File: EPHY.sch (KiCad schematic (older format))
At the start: 10 parts

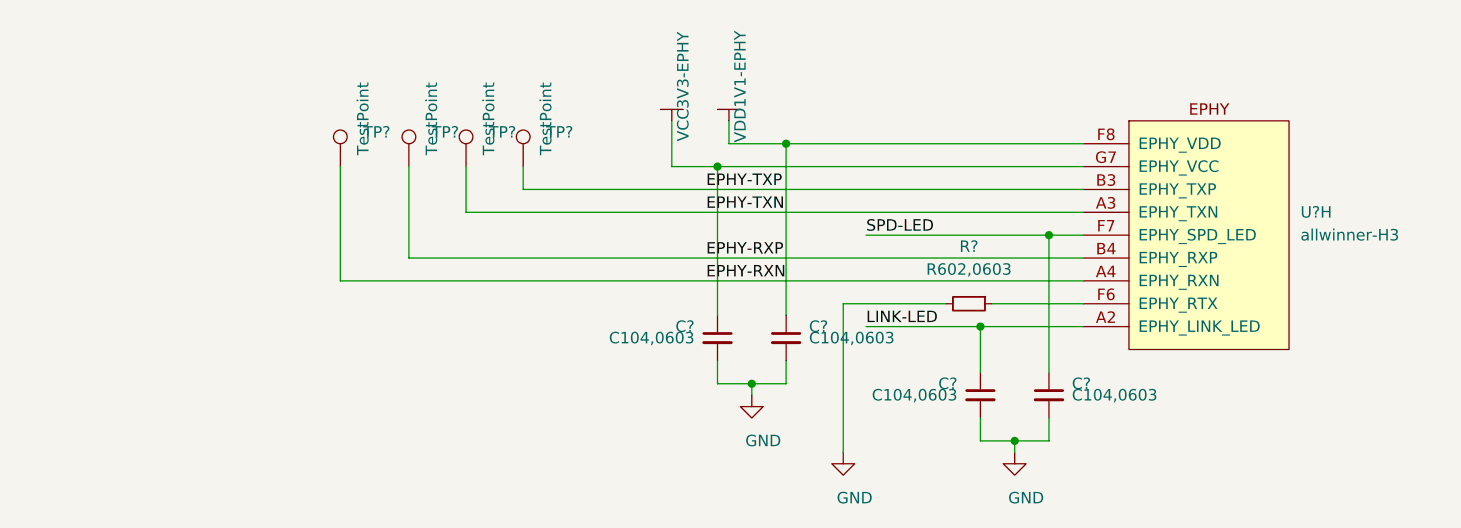
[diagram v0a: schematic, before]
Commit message: update test point,
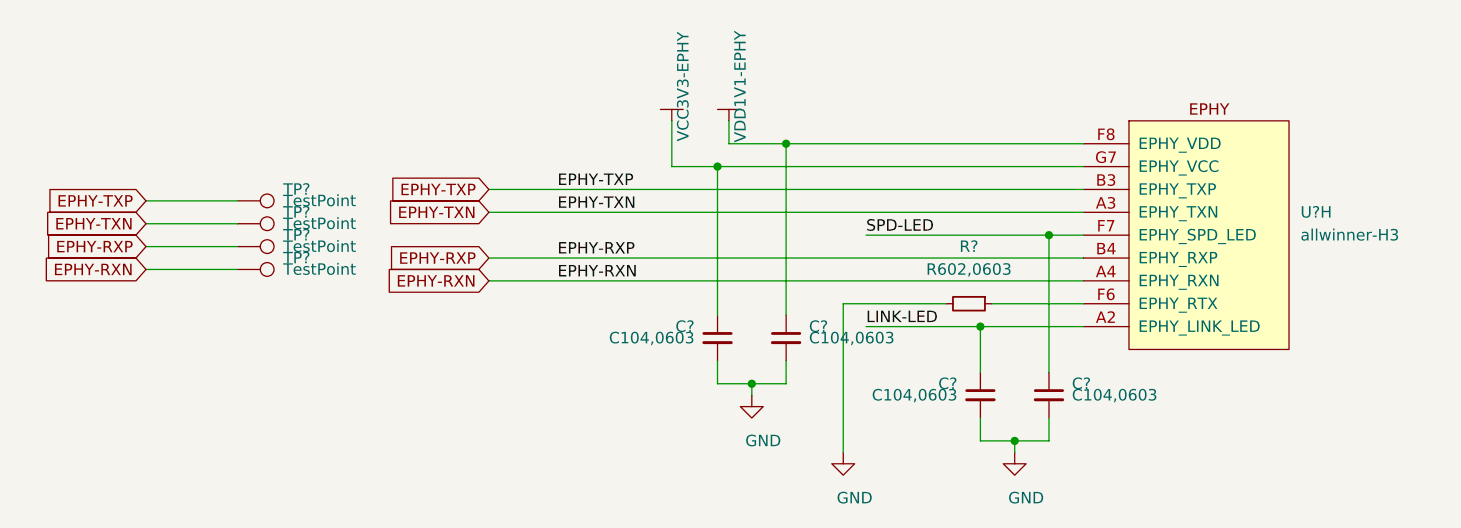
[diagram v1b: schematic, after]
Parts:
- removed TP? (x4): TestPoint, symbol Connector:TestPoint
- added TP? (x4): TestPoint, symbol Connector:TestPoint
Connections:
- net EPHY-RXN: now also TP?.1
- net EPHY-RXP: now also TP?.1
- net EPHY-TXN: now also TP?.1
- net EPHY-TXP: now also TP?.1
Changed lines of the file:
@@
 	1    0    0    -1
 $EndComp
-$Comp
-L Connector:TestPoint TP?
-U 1 1 5C29337F
-P 6550 3850
-AR Path="/5C273FE9/5C2931D3/5C29337F" Ref="TP?"  Part="1"
-AR Path="/5C273FE9/5C29E760/5C29337F" Ref="TP?"  Part="1"
-AR Path="/5C7B767A/5C2931D3/5C29337F" Ref="TP?"  Part="1"
-F 0 "TP?" H 6650 4000 50  0000 L CNN
-F 1 "TestPoint" V 6650 3900 50  0000 L CNN
-F 2 "" H 6750 3850 50  0001 C CNN
-F 3 "~" H 6750 3850 50  0001 C CNN
-	1    6550 3850
-	1    0    0    -1
-$EndComp
-$Comp
-L Connector:TestPoint TP?
-U 1 1 5C29348D
-P 6300 3850
-AR Path="/5C273FE9/5C2931D3/5C29348D" Ref="TP?"  Part="1"
-AR Path="/5C273FE9/5C29E760/5C29348D" Ref="TP?"  Part="1"
-AR Path="/5C7B767A/5C2931D3/5C29348D" Ref="TP?"  Part="1"
-F 0 "TP?" H 6400 4000 50  0000 L CNN
-F 1 "TestPoint" V 6400 3900 50  0000 L CNN
-F 2 "" H 6500 3850 50  0001 C CNN
-F 3 "~" H 6500 3850 50  0001 C CNN
-	1    6300 3850
-	1    0    0    -1
-$EndComp
-$Comp
-L Connector:TestPoint TP?
-U 1 1 5C2934A9
-P 6050 3850
-AR Path="/5C273FE9/5C2931D3/5C2934A9" Ref="TP?"  Part="1"
-AR Path="/5C273FE9/5C29E760/5C2934A9" Ref="TP?"  Part="1"
-AR Path="/5C7B767A/5C2931D3/5C2934A9" Ref="TP?"  Part="1"
-F 0 "TP?" H 6150 4000 50  0000 L CNN
-F 1 "TestPoint" V 6150 3900 50  0000 L CNN
-F 2 "" H 6250 3850 50  0001 C CNN
-F 3 "~" H 6250 3850 50  0001 C CNN
-	1    6050 3850
-	1    0    0    -1
-$EndComp
-$Comp
-L Connector:TestPoint TP?
-U 1 1 5C2934C7
-P 5750 3850
-AR Path="/5C273FE9/5C2931D3/5C2934C7" Ref="TP?"  Part="1"
-AR Path="/5C273FE9/5C29E760/5C2934C7" Ref="TP?"  Part="1"
-AR Path="/5C7B767A/5C2931D3/5C2934C7" Ref="TP?"  Part="1"
-F 0 "TP?" H 5850 4000 50  0000 L CNN
-F 1 "TestPoint" V 5850 3900 50  0000 L CNN
-F 2 "" H 5950 3850 50  0001 C CNN
-F 3 "~" H 5950 3850 50  0001 C CNN
-	1    5750 3850
-	1    0    0    -1
-$EndComp
-Wire Wire Line
-	9000 4250 6050 4250
-Wire Wire Line
-	6050 4250 6050 3850
-Wire Wire Line
-	9000 4350 5750 4350
-Wire Wire Line
-	5750 4350 5750 3850
-Wire Wire Line
-	9000 3950 6550 3950
-Wire Wire Line
-	6550 3950 6550 3850
-Wire Wire Line
-	9000 4050 6300 4050
-Wire Wire Line
-	6300 4050 6300 3850
-Text Label 7350 4250 0    50   ~ 0
+Text Label 6700 4250 0    50   ~ 0
 EPHY-RXP
-Text Label 7350 4350 0    50   ~ 0
+Text Label 6700 4350 0    50   ~ 0
 EPHY-RXN
-Text Label 7350 3950 0    50   ~ 0
+Text Label 6700 3950 0    50   ~ 0
 EPHY-TXP
-Text Label 7350 4050 0    50   ~ 0
+Text Label 6700 4050 0    50   ~ 0
 EPHY-TXN
 $Comp
@@
 Wire Wire Line
 	7950 4450 8400 4450
+Wire Wire Line
+	6400 3950 9000 3950
+Wire Wire Line
+	6400 4050 9000 4050
+Wire Wire Line
+	6400 4250 9000 4250
+Wire Wire Line
+	6400 4350 9000 4350
+Text GLabel 6400 3950 0    50   Input ~ 0
+EPHY-TXP
+Text GLabel 6400 4050 0    50   Input ~ 0
+EPHY-TXN
+Text GLabel 6400 4250 0    50   Input ~ 0
+EPHY-RXP
+Text GLabel 6400 4350 0    50   Input ~ 0
+EPHY-RXN
+Text GLabel 4900 4000 0    50   Input ~ 0
+EPHY-TXP
+Text GLabel 4900 4100 0    50   Input ~ 0
+EPHY-TXN
+Text GLabel 4900 4200 0    50   Input ~ 0
+EPHY-RXP
+Text GLabel 4900 4300 0    50   Input ~ 0
+EPHY-RXN
+$Comp
+L Connector:TestPoint TP?
+U 1 1 5C3417E1
+P 5300 4000
+F 0 "TP?" V 5250 4200 50  0000 L CNN
+F 1 "TestPoint" V 5300 4200 50  0000 L CNN
+F 2 "" H 5500 4000 50  0001 C CNN
+F 3 "~" H 5500 4000 50  0001 C CNN
+	1    5300 4000
+	0    1    1    0
+$EndComp
+$Comp
+L Connector:TestPoint TP?
+U 1 1 5C34247F
+P 5300 4100
+F 0 "TP?" V 5250 4300 50  0000 L CNN
+F 1 "TestPoint" V 5300 4300 50  0000 L CNN
+F 2 "" H 5500 4100 50  0001 C CNN
+F 3 "~" H 5500 4100 50  0001 C CNN
+	1    5300 4100
+	0    1    1    0
+$EndComp
+$Comp
+L Connector:TestPoint TP?
+U 1 1 5C34249F
+P 5300 4200
+F 0 "TP?" V 5250 4400 50  0000 L CNN
+F 1 "TestPoint" V 5300 4400 50  0000 L CNN
+F 2 "" H 5500 4200 50  0001 C CNN
+F 3 "~" H 5500 4200 50  0001 C CNN
+	1    5300 4200
+	0    1    1    0
+$EndComp
+$Comp
+L Connector:TestPoint TP?
+U 1 1 5C3424C1
+P 5300 4300
+F 0 "TP?" V 5250 4500 50  0000 L CNN
+F 1 "TestPoint" V 5300 4500 50  0000 L CNN
+F 2 "" H 5500 4300 50  0001 C CNN
+F 3 "~" H 5500 4300 50  0001 C CNN
+	1    5300 4300
+	0    1    1    0
+$EndComp
+Wire Wire Line
+	4900 4000 5300 4000
+Wire Wire Line
+	4900 4100 5300 4100
+Wire Wire Line
+	4900 4200 5300 4200
+Wire Wire Line
+	4900 4300 5300 4300
 $EndSCHEMATC
